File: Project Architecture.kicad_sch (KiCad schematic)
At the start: 0 parts

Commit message: Testing new path for custom 3D model
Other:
- sheet Section A - Title A renamed Schematic
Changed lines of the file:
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@@
 			(color 128 255 128 0.5000)
 		)
-		(property "Sheetname" "Section A - Title A"
+		(property "Sheetname" "Schematic"
 			(at 190.5 75.1709 0)
 			(effects

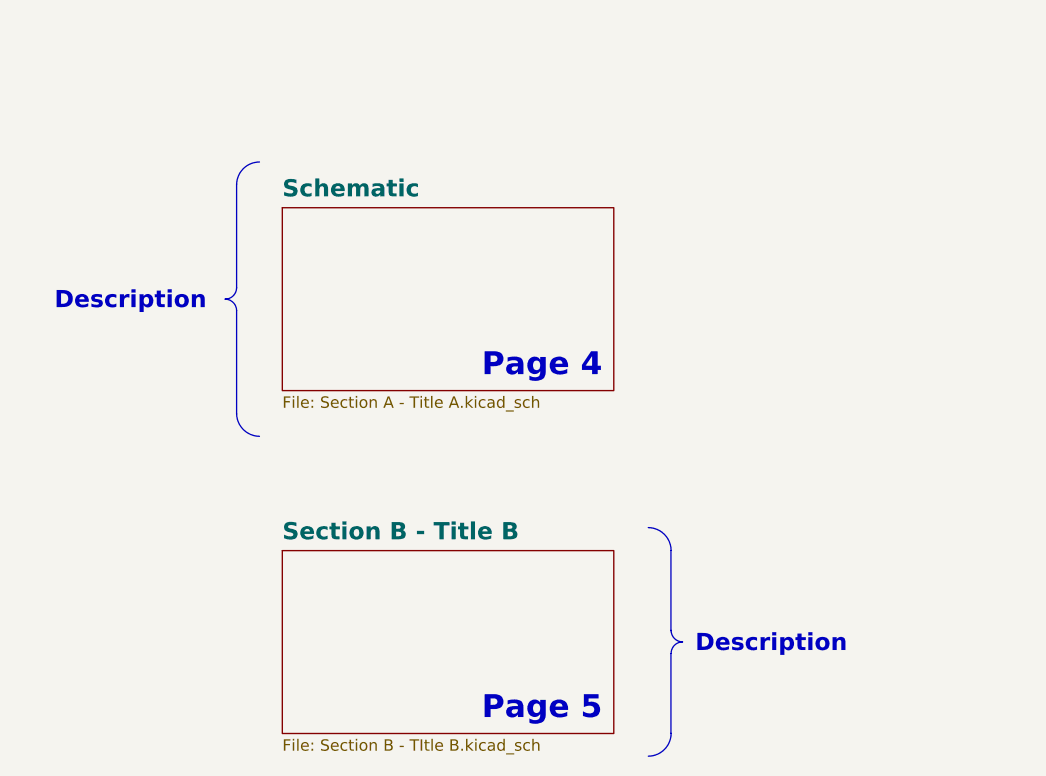
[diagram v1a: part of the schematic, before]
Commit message: New 3D path for trafo
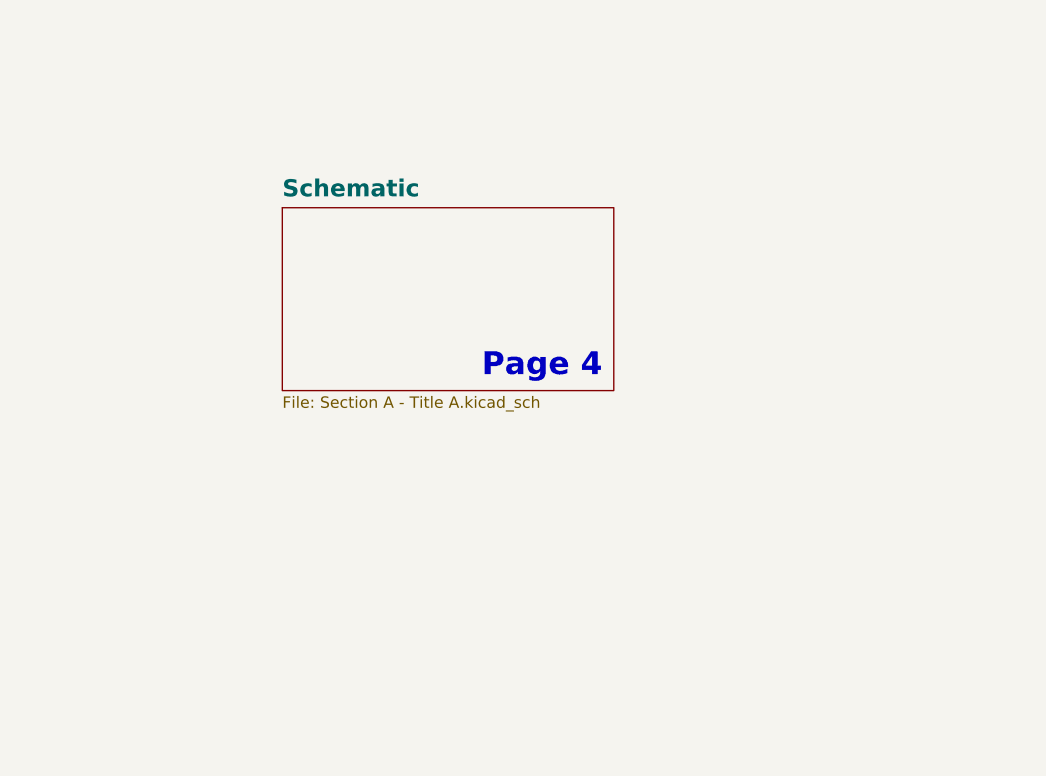
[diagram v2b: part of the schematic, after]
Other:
- removed sheet Section B - Title B
- note removed: "Page 5"
